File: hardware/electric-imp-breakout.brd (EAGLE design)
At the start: 32.1 x 50.8 mm, 22 parts, among them Q1 DMG2307L-7, U1 ELECTRIC_IMP, U2 TPS62172, U3 ATSHA204-TSU, X1 USBSMD

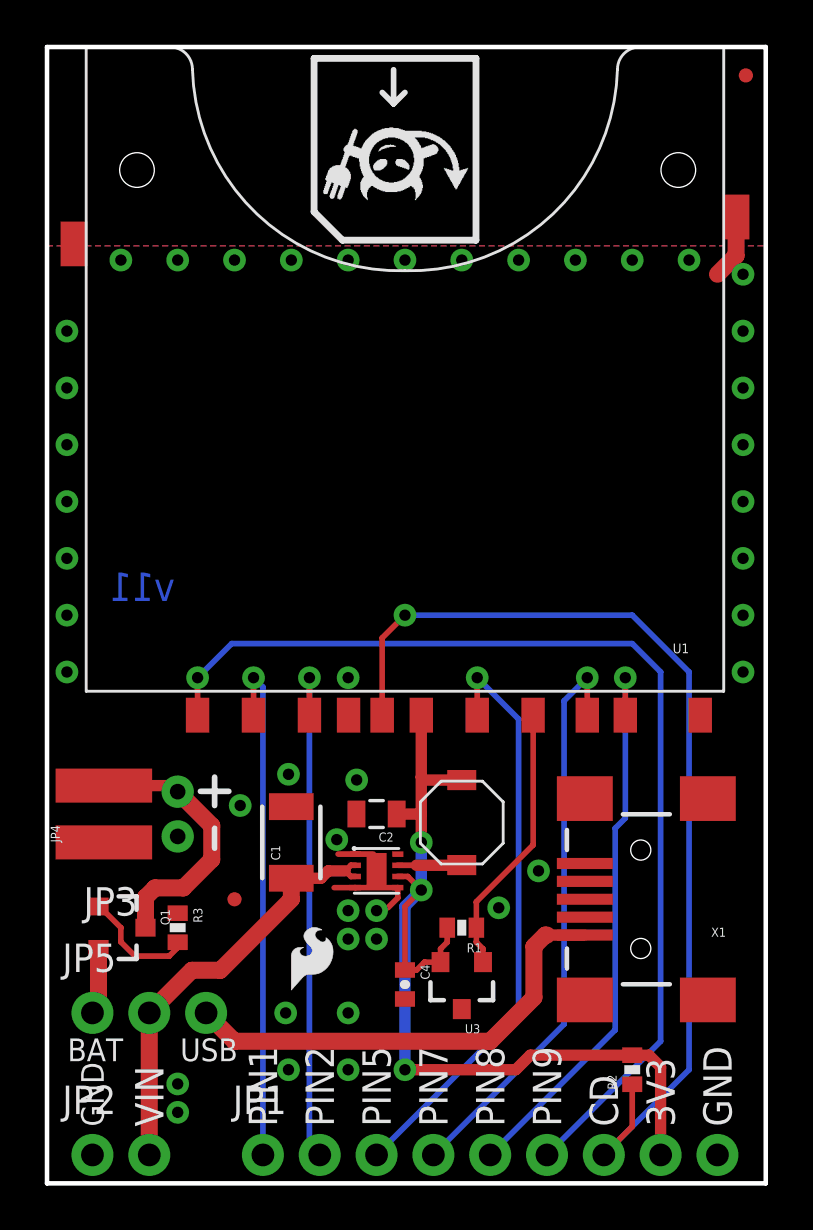
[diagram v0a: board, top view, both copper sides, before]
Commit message: Changing to new socket FP, 0603 components, schematic updates
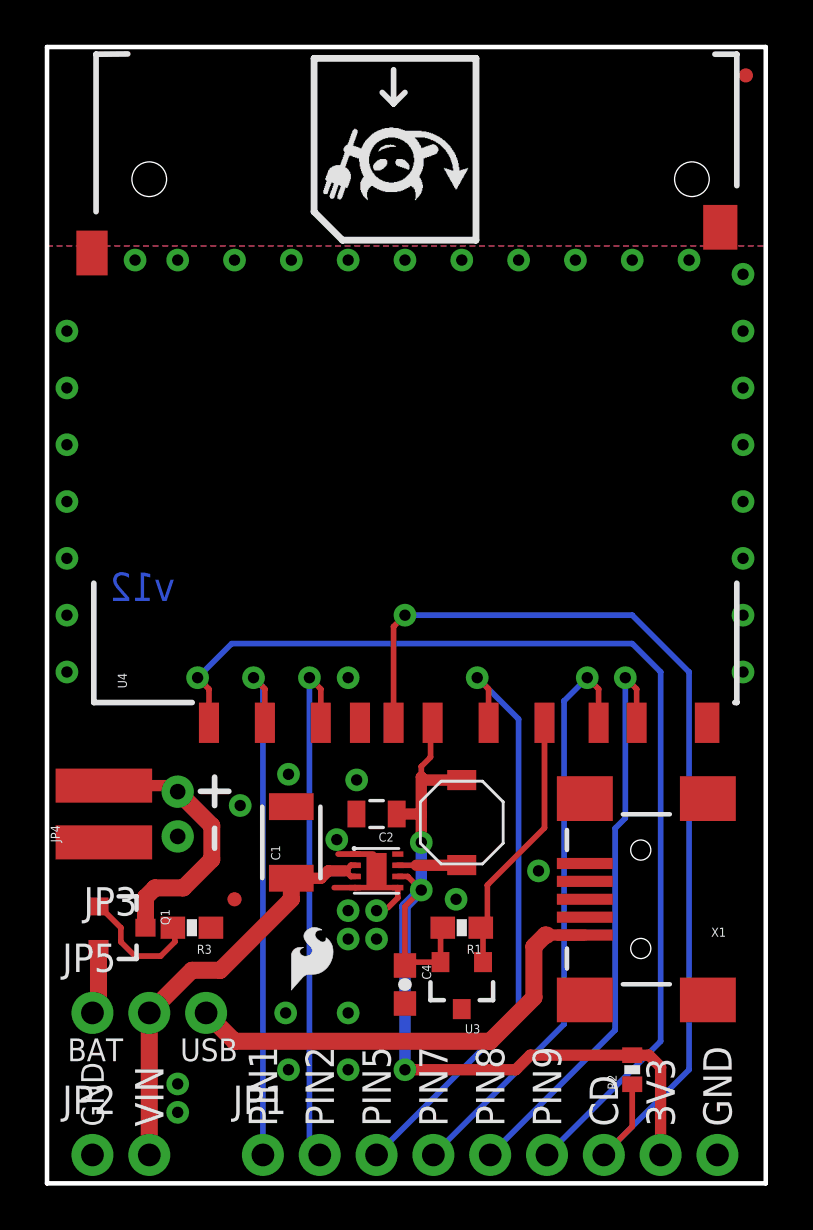
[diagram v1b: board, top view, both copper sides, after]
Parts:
- removed U1: ELECTRIC_IMP, SparkFun-RF:SD_MMC_SOCKET
- added FRAME1: FRAME-LETTER, SparkFun-Retired:CREATIVE_COMMONS
- added U$3: REVISION, SparkFun-Aesthetics:REVISION
- added U4: ELECTRIC_IMP, SparkFun-RF:SD_1:1
- C1: device SparkFun-Passives:1210 -> SparkFun-Capacitors:1210
- C2: device SparkFun-Passives:0805 -> SparkFun-Capacitors:0805
- C4: device SparkFun-Passives:0402-CAP -> SparkFun-Capacitors:0603-CAP
- R1, R3: device SparkFun-Passives:0402-RES -> SparkFun-Resistors:0603-RES
- moved R3 0.64 mm to (6.48, 11.4), turned to 180 degrees
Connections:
- net 3.3V: now also U4.4; no longer U1.4
- net CD: now also U4.CD; no longer U1.CD
- net GND: now also U4.3, U4.SH@1, U4.SH@2; no longer U1.3, U1.S1, U1.S2
- net ID: now also U4.6; no longer U1.6
- net PIN1: now also U4.1; no longer U1.1
- net PIN2: now also U4.2; no longer U1.2
- net PIN5: now also U4.5; no longer U1.5
- net PIN7: now also U4.7; no longer U1.7
- net PIN8: now also U4.8; no longer U1.8
- net PIN9: now also U4.9; no longer U1.9
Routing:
- net GND: track 8.46 -> 5.56 mm
- net PIN8: track 25.6 -> 26.1 mm
- net PIN7: track 25.9 -> 26.4 mm
- net PIN5: track 26.4 -> 27.0 mm
- net PIN2: track 23.2 -> 23.8 mm
- net PIN1: track 23.2 -> 23.7 mm
- net PIN9: track 47.2 -> 47.8 mm
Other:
- board text added: "Electric Imp (based on their April design)"
- board text added: "Jim Lindblom"
- board text added: "Toni Klopfenstein"
- board text added: "v12"
- board text removed: "v11"

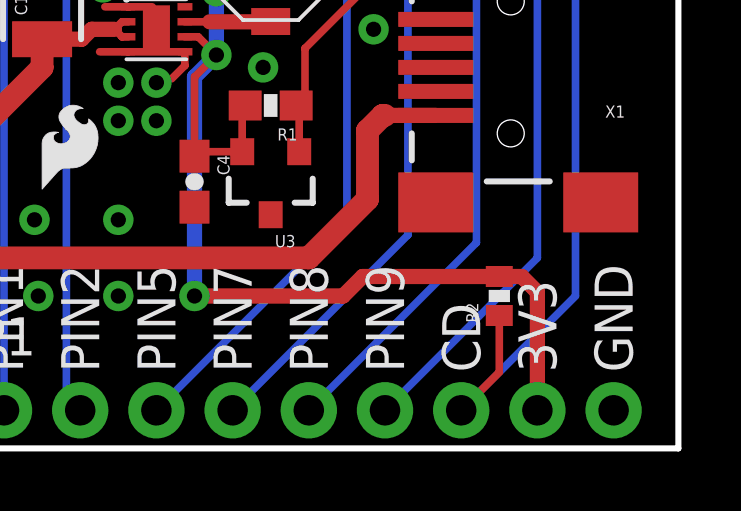
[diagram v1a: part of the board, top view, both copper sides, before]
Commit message: Fixing DNP resistor to 0603, changing sparkfun logo
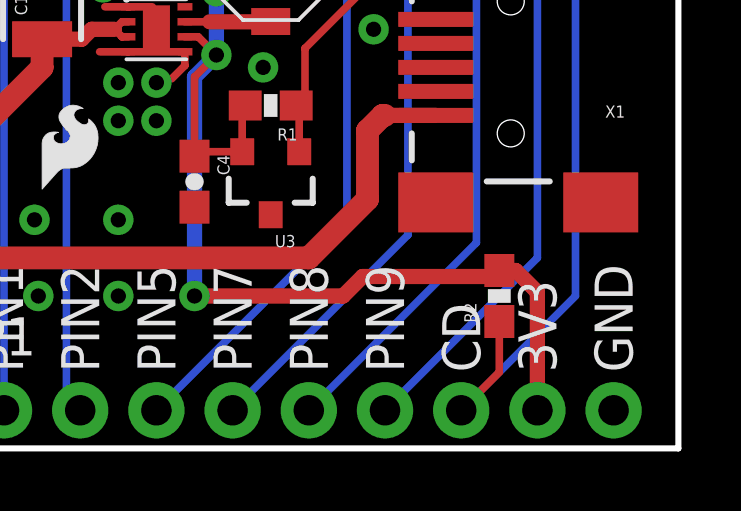
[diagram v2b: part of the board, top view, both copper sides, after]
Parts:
- JP7: value LOGO-SFENEW -> SFE_LOGO_NAME_FLAME.1_INCH; device SparkFun-Aesthetics:SFE-NEW-WEBLOGO -> SparkFun-Aesthetics:SFE_LOGO_NAME_FLAME_.1
- R2: device SparkFun-Passives:0402-RES -> SparkFun-Resistors:0603-RES
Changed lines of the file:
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@@
 <setting verticaltext="up"/>
 </settings>
-<grid distance="0.025" unitdist="inch" unit="inch" style="lines" multiple="1" display="yes" altdistance="0.005" altunitdist="inch" altunit="inch"/>
+<grid distance="0.05" unitdist="inch" unit="inch" style="lines" multiple="1" display="yes" altdistance="0.005" altunitdist="inch" altunit="inch"/>
 <layers>
 <layer number="1" name="Top" color="4" fill="1" visible="yes" active="yes"/>
@@
 <layer number="108" name="tplace-old" color="10" fill="1" visible="no" active="yes"/>
 <layer number="109" name="ref-old" color="11" fill="1" visible="no" active="yes"/>
-<layer number="110" name="fp0" color="7" fill="1" visible="yes" active="yes"/>
-<layer number="111" name="LPC17xx" color="7" fill="1" visible="yes" active="yes"/>
-<layer number="112" name="tSilk" color="7" fill="1" visible="yes" active="yes"/>
-<layer number="113" name="IDFDebug" color="4" fill="1" visible="yes" active="yes"/>
+<layer number="110" name="fp0" color="7" fill="1" visible="no" active="yes"/>
+<layer number="111" name="LPC17xx" color="7" fill="1" visible="no" active="yes"/>
+<layer number="112" name="tSilk" color="7" fill="1" visible="no" active="yes"/>
+<layer number="113" name="IDFDebug" color="4" fill="1" visible="no" active="yes"/>
 <layer number="116" name="Patch_BOT" color="9" fill="4" visible="no" active="yes"/>
 <layer number="121" name="_tsilk" color="7" fill="1" visible="no" active="yes"/>
 <layer number="122" name="_bsilk" color="7" fill="1" visible="no" active="yes"/>
-<layer number="123" name="tTestmark" color="7" fill="1" visible="yes" active="yes"/>
-<layer number="124" name="bTestmark" color="7" fill="1" visible="yes" active="yes"/>
+<layer number="123" name="tTestmark" color="7" fill="1" visible="no" active="yes"/>
+<layer number="124" name="bTestmark" color="7" fill="1" visible="no" active="yes"/>
 <layer number="125" name="_tNames" color="7" fill="1" visible="no" active="yes"/>
-<layer number="126" name="_bNames" color="7" fill="1" visible="yes" active="yes"/>
-<layer number="127" name="_tValues" color="7" fill="1" visible="yes" active="yes"/>
-<layer number="128" name="_bValues" color="7" fill="1" visible="yes" active="yes"/>
-<layer number="131" name="tAdjust" color="7" fill="1" visible="yes" active="yes"/>
-<layer number="132" name="bAdjust" color="7" fill="1" visible="yes" active="yes"/>
+<layer number="126" name="_bNames" color="7" fill="1" visible="no" active="yes"/>
+<layer number="127" name="_tValues" color="7" fill="1" visible="no" active="yes"/>
+<layer number="128" name="_bValues" color="7" fill="1" visible="no" active="yes"/>
+<layer number="131" name="tAdjust" color="7" fill="1" visible="no" active="yes"/>
+<layer number="132" name="bAdjust" color="7" fill="1" visible="no" active="yes"/>
 <layer number="144" name="Drill_legend" color="7" fill="1" visible="no" active="yes"/>
-<layer number="150" name="Notes" color="7" fill="1" visible="yes" active="yes"/>
+<layer number="150" name="Notes" color="7" fill="1" visible="no" active="yes"/>
 <layer number="151" name="HeatSink" color="7" fill="1" visible="no" active="yes"/>
-<layer number="152" name="_bDocu" color="7" fill="1" visible="yes" active="yes"/>
-<layer number="153" name="FabDoc1" color="7" fill="1" visible="yes" active="yes"/>
-<layer number="154" name="FabDoc2" color="7" fill="1" visible="yes" active="yes"/>
-<layer number="155" name="FabDoc3" color="7" fill="1" visible="yes" active="yes"/>
-<layer number="199" name="Contour" color="7" fill="1" visible="yes" active="yes"/>
+<layer number="152" name="_bDocu" color="7" fill="1" visible="no" active="yes"/>
+<layer number="153" name="FabDoc1" color="7" fill="1" visible="no" active="yes"/>
+<layer number="154" name="FabDoc2" color="7" fill="1" visible="no" active="yes"/>
+<layer number="155" name="FabDoc3" color="7" fill="1" visible="no" active="yes"/>
+<layer number="199" name="Contour" color="7" fill="1" visible="no" active="yes"/>
 <layer number="200" name="200bmp" color="1" fill="10" visible="no" active="yes"/>
 <layer number="201" name="201bmp" color="2" fill="10" visible="no" active="yes"/>
@@
 <layer number="223" name="223bmp" color="24" fill="1" visible="no" active="no"/>
 <layer number="224" name="224bmp" color="25" fill="1" visible="no" active="no"/>
-<layer number="248" name="Housing" color="7" fill="1" visible="yes" active="yes"/>
-<layer number="249" name="Edge" color="7" fill="1" visible="yes" active="yes"/>
+<layer number="248" name="Housing" color="7" fill="1" visible="no" active="yes"/>
+<layer number="249" name="Edge" color="7" fill="1" visible="no" active="yes"/>
 <layer number="250" name="Descript" color="3" fill="1" visible="no" active="no"/>
 <layer number="251" name="SMDround" color="12" fill="11" visible="no" active="no"/>
@@
 <element name="JP1" library="SparkFun-Connectors" package="1X09_NO_SILK" value="M09NO_SILK" x="9.652" y="1.27"/>
 <element name="JP2" library="SparkFun-Connectors" package="1X02_NO_SILK" value="" x="2.032" y="1.27"/>
-<element name="R2" library="SparkFun-Passives" package="0402-RES" value="dnp" x="26.162" y="5.08" rot="R90"/>
+<element name="R2" library="SparkFun-Resistors" package="0603-RES" value="dnp" x="26.162" y="5.08" rot="R90"/>
 <element name="X1" library="SparkFun-Connectors" package="USB-MINIB" value="USBSMD" x="26.543" y="12.7" rot="R180"/>
 <element name="JP4" library="SparkFun-Connectors" package="JST-2-PTH-NS" value="" x="5.842" y="16.51" rot="R90"/>
@@
 <element name="JP3" library="SparkFun-Connectors" package="1X02_SMD" value="" x="2.54" y="16.51" rot="R180"/>
 <element name="JP6" library="SparkFun-Aesthetics" package="SFE-LOGO-FLAME" value="LOGO-SFESK" x="10.922" y="8.636"/>
-<element name="JP7" library="SparkFun-Aesthetics" package="SFE-NEW-WEBLOGO" value="LOGO-SFENEW" x="20.574" y="35.306" rot="MR0"/>
+<element name="JP7" library="SparkFun-Aesthetics" package="SFE_LOGO_NAME_FLAME_.1" value="SFE_LOGO_NAME_FLAME.1_INCH" x="20.574" y="35.306" rot="MR0"/>
 <element name="U$5" library="SparkFun-Aesthetics" package="OSHW-LOGO-S" value="OSHW-LOGOS" x="4.191" y="28.702" rot="MR0"/>
 <element name="JP8" library="SparkFun" package="MICRO-FIDUCIAL" value="FIDUCIALUFIDUCIAL" x="31.242" y="49.53"/>
@@
 <wire x1="16.002" y1="5.08" x2="16.002" y2="12.383" width="0.508" layer="16"/>
 <wire x1="16.002" y1="12.383" x2="16.002" y2="9.74" width="0.254" layer="1"/>
-<wire x1="26.162" y1="5.73" x2="21.605" y2="5.73" width="0.508" layer="1"/>
 <wire x1="21.605" y1="5.73" x2="20.955" y2="5.08" width="0.508" layer="1"/>
 <wire x1="20.955" y1="5.08" x2="16.002" y2="5.08" width="0.508" layer="1"/>
 <wire x1="27.432" y1="1.27" x2="27.432" y2="5.207" width="0.508" layer="1"/>
-<wire x1="27.432" y1="5.207" x2="26.909" y2="5.73" width="0.508" layer="1"/>
-<wire x1="26.162" y1="5.73" x2="26.909" y2="5.73" width="0.508" layer="1"/>
 <via x="16.732" y="15.24" extent="1-16" drill="0.508"/>
 <wire x1="16.732" y1="15.24" x2="16.732" y2="13.113" width="0.508" layer="16"/>
@@
 <wire x1="17.592" y1="9.89" x2="17.592" y2="11.33" width="0.254" layer="1"/>
 <wire x1="17.592" y1="11.33" x2="17.692" y2="11.43" width="0.254" layer="1"/>
+<wire x1="21.605" y1="5.73" x2="25.962" y2="5.73" width="0.508" layer="1"/>
+<wire x1="25.962" y1="5.73" x2="26.162" y2="5.93" width="0.508" layer="1"/>
+<wire x1="26.162" y1="5.93" x2="26.709" y2="5.93" width="0.508" layer="1"/>
+<wire x1="26.709" y1="5.93" x2="27.432" y2="5.207" width="0.508" layer="1"/>
 </signal>
 <signal name="ID">
@@
 <contactref element="R2" pad="1"/>
 <wire x1="24.892" y1="1.27" x2="26.162" y2="2.54" width="0.254" layer="1"/>
-<wire x1="26.162" y1="2.54" x2="26.162" y2="4.43" width="0.254" layer="1"/>
+<wire x1="26.162" y1="2.54" x2="26.162" y2="4.23" width="0.254" layer="1"/>
 <via x="16.002" y="25.4" extent="1-16" drill="0.508"/>
 <wire x1="16.002" y1="25.4" x2="26.162" y2="25.4" width="0.254" layer="16"/>

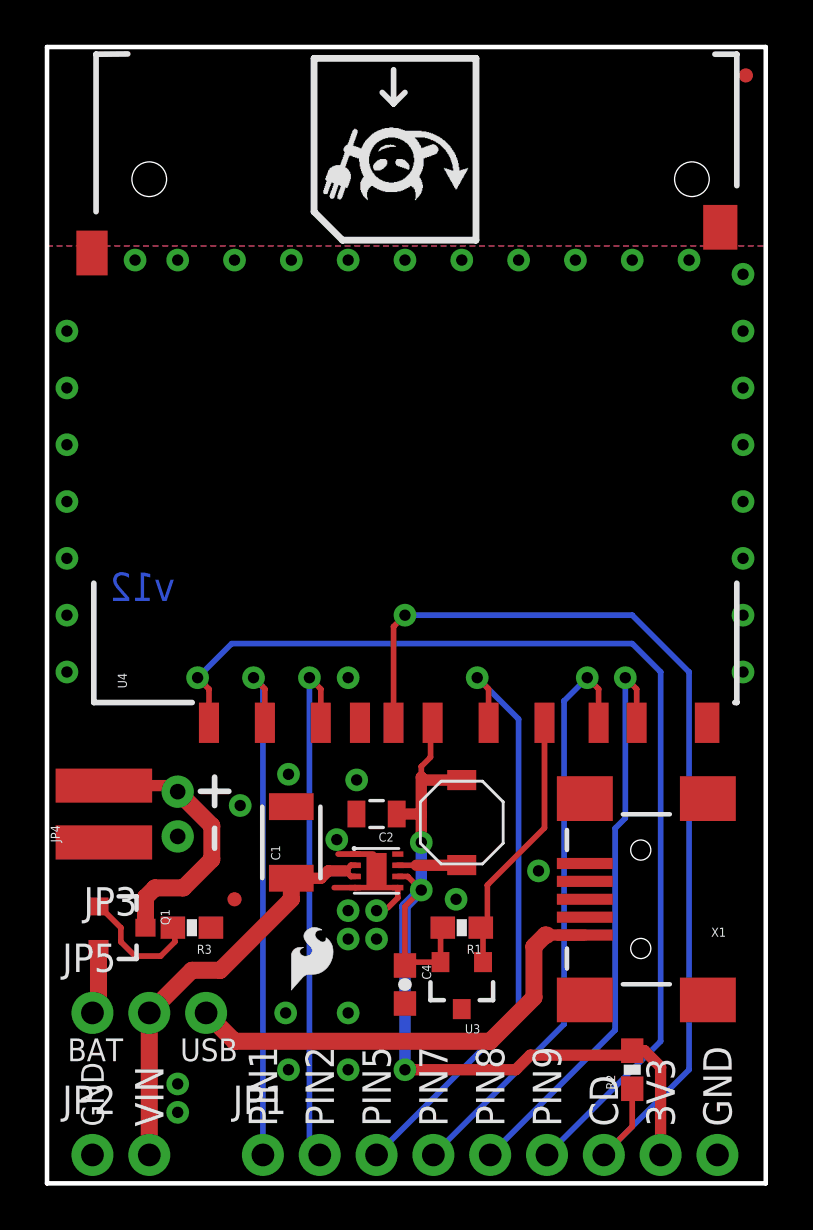
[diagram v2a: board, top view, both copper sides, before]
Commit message: removed micro fids, added regular
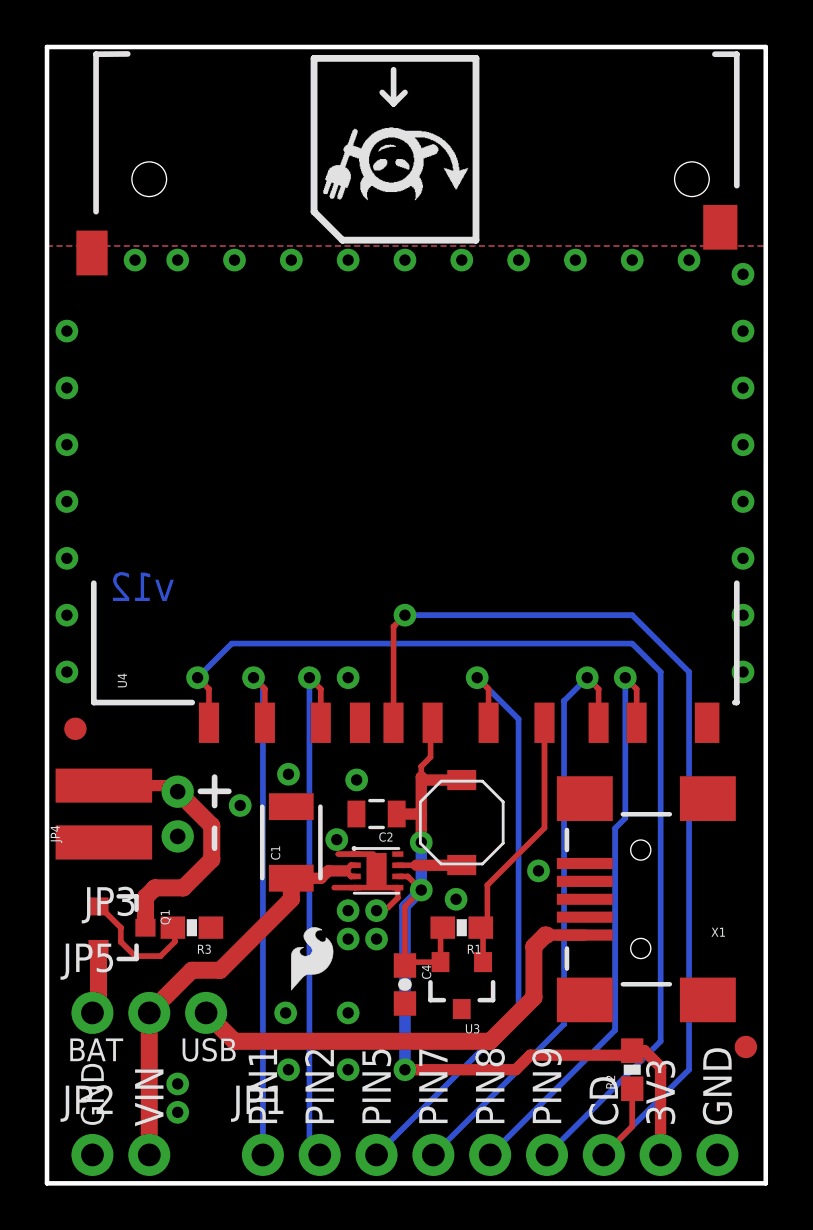
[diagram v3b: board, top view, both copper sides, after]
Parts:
- removed JP8, JP9: FIDUCIALUFIDUCIAL, SparkFun:MICRO-FIDUCIAL
- added FID1, FID2: FIDUCIAL1X2, SparkFun-Aesthetics:FIDUCIAL-1X2
